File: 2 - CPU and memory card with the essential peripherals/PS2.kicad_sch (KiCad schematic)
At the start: 7 parts, among them J10 KEYBOARD, J11 MOUSE, U16 VT82C42, U17 74LS06

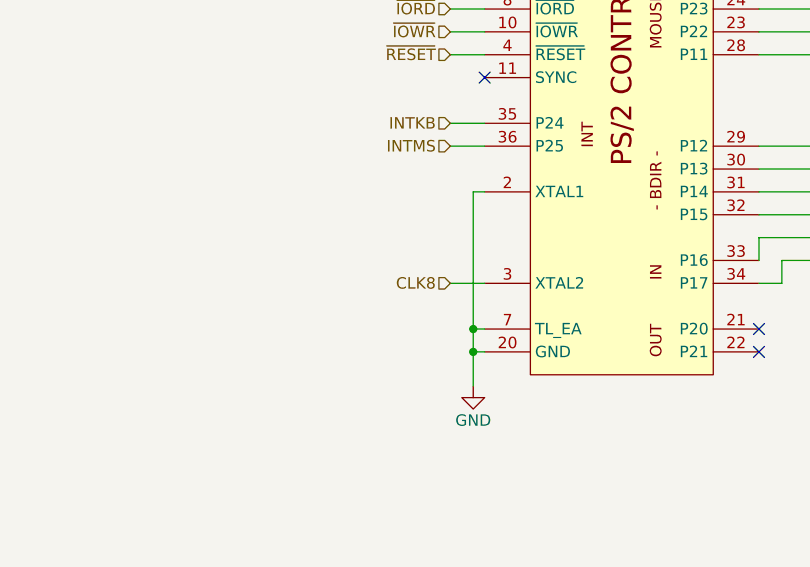
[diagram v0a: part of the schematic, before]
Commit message: Added existing assembler code and PLD files
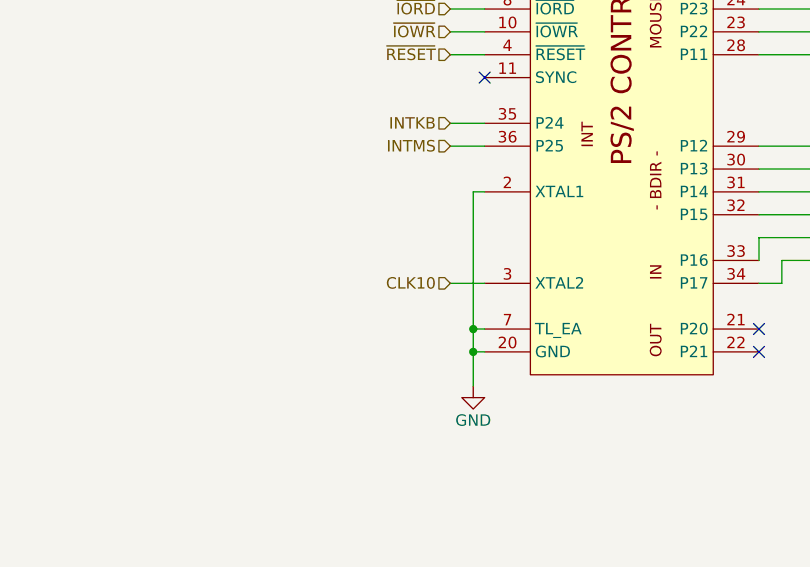
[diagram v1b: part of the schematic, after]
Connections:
- net CLK8 renamed CLK10
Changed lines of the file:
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@@
     (effects (font (size 1.27 1.27)) (justify right))
   )
-  (hierarchical_label "CLK8" (shape input) (at 91.44 120.65 180) (fields_autoplaced)
+  (hierarchical_label "CLK10" (shape input) (at 91.44 120.65 180) (fields_autoplaced)
     (effects (font (size 1.27 1.27)) (justify right))
   )
